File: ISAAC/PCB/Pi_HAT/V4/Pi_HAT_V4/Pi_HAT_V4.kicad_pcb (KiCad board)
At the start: 2 copper layers, 71.7 x 71.3 mm, 29 parts, among them J1 MPU 6050, J2 Pi_GPIO, J3 Display, J4 Conn_01x04_Male, J5 XT60PW-M, J6 Conn_01x04_Male, J8 XT60PW-M, U1 MP2315GJ-Z

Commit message: Updated code: Sorta works
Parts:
- added J7: Pressure Sensor, Connector_PinHeader_2.54mm:PinHeader_1x03_P2.54mm_Vertical, F.Cu at (96.5, 83.9)
- added R1: 2k, Resistor_SMD:R_0805_2012Metric_Pad1.20x1.40mm_HandSolder, B.Cu at (128.4, 96.7)
- added R6: 1k, Resistor_SMD:R_0805_2012Metric_Pad1.20x1.40mm_HandSolder, B.Cu at (130.7, 96.7)
- added R7: 2k, Resistor_SMD:R_0805_2012Metric_Pad1.20x1.40mm_HandSolder, B.Cu at (126.6, 92.2)
- added R8: 1k, Resistor_SMD:R_0805_2012Metric_Pad1.20x1.40mm_HandSolder, B.Cu at (129.0, 92.2)
- added U2: MCP3008-I/SL, .pretty:SOIC127P600X175-16N, B.Cu at (137.5, 93.7)
- moved G*** 3.54 mm to (138.1, 92.5), turned to -45 degrees
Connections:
- C1 pad 1: /Buck Converter/12V -> /12V1
- C2 pad 1: /Buck Converter/12V -> /12V1
- J2 pad 19: unconnected-(J2-Pin_19-Pad19) -> /MOSI
- J2 pad 21: unconnected-(J2-Pin_21-Pad21) -> /MISO
- J2 pad 23: unconnected-(J2-Pin_23-Pad23) -> /SCLK
- J2 pad 24: unconnected-(J2-Pin_24-Pad24) -> /CS
- J4 pad 1: /Buck Converter/12V -> /12V0
- J5 pad 1: /Buck Converter/12V -> /12V0
- J6 pad 1: /Buck Converter/12V -> /12V0
- J8 pad 1: /Buck Converter/12V -> /12V1
- R2 pad 1: /Buck Converter/12V -> /12V1
- U1 pad 2: /Buck Converter/12V -> /12V1
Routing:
- net /Buck Converter/12V: track 189.7 -> 0.00 mm
- net /12V0: track 0.00 -> 138.0 mm
- net /12V1: track 0.00 -> 68.0 mm, vias 0 -> 2
- net GND: track 106.6 -> 150.5 mm
- net /5V: track 85.9 -> 125.7 mm
- net /PS: track 0.00 -> 37.5 mm, vias 0 -> 1
- net /CS: track 0.00 -> 21.6 mm, vias 0 -> 1
- net /SCLK: track 0.00 -> 21.4 mm, vias 0 -> 1
- net /MISO: track 0.00 -> 19.7 mm, vias 0 -> 1
- net /MOSI: track 0.00 -> 18.0 mm, vias 0 -> 1
- net /3.3V: track 68.0 -> 80.1 mm
- net /A-D Converter/4V1: track 0.00 -> 10.1 mm
- net /A-D Converter/4V0: track 0.00 -> 9.49 mm
- added copper zone on B.Cu, net GND
- removed copper zone on F.Cu, net GND
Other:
- board text added: "PI HAT V3 10/21/22 EASY CONTROLS Designed by: Jacob Romeo"
- board text added: "PS"
- board text removed: "PI HAT V4 05/05/23 EASY CONTROLS Designed by: Jacob Romeo"

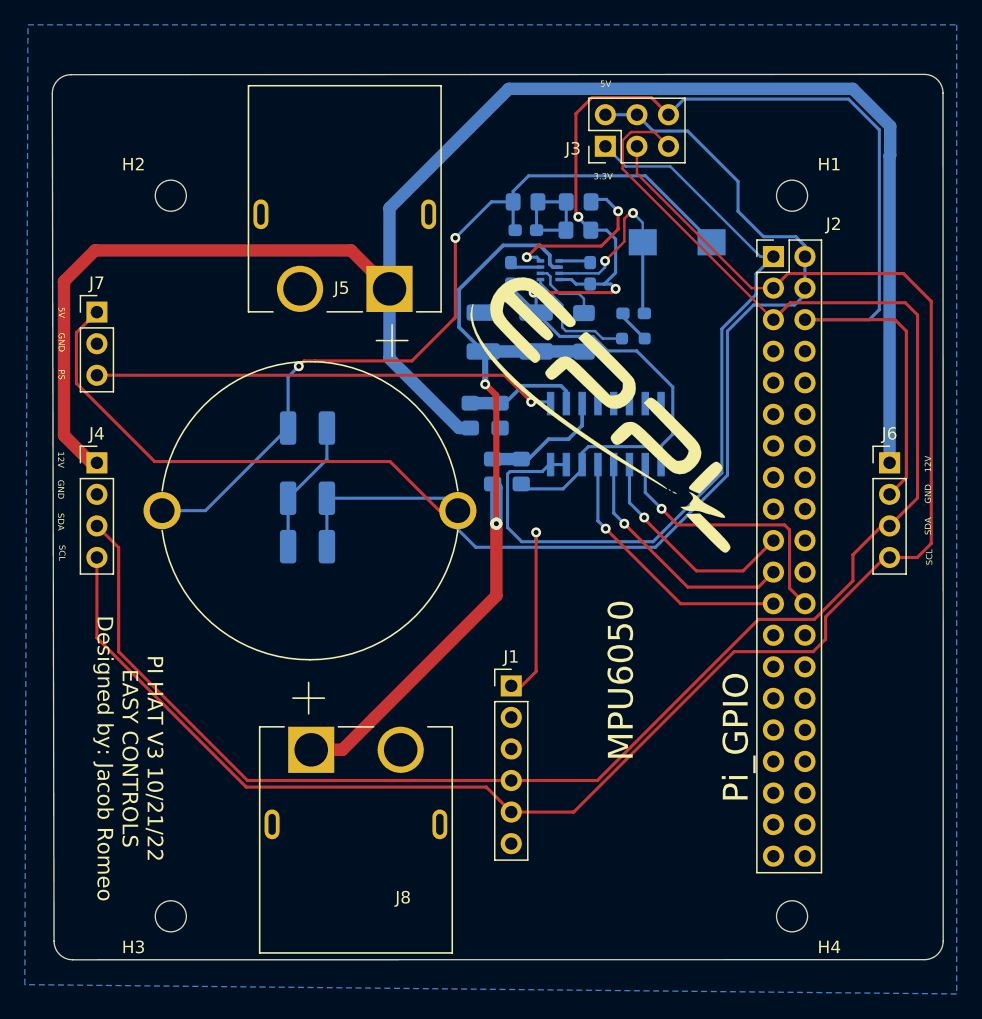
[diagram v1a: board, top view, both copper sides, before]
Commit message: Updated
Started SPARK grant and updated controller and PCB
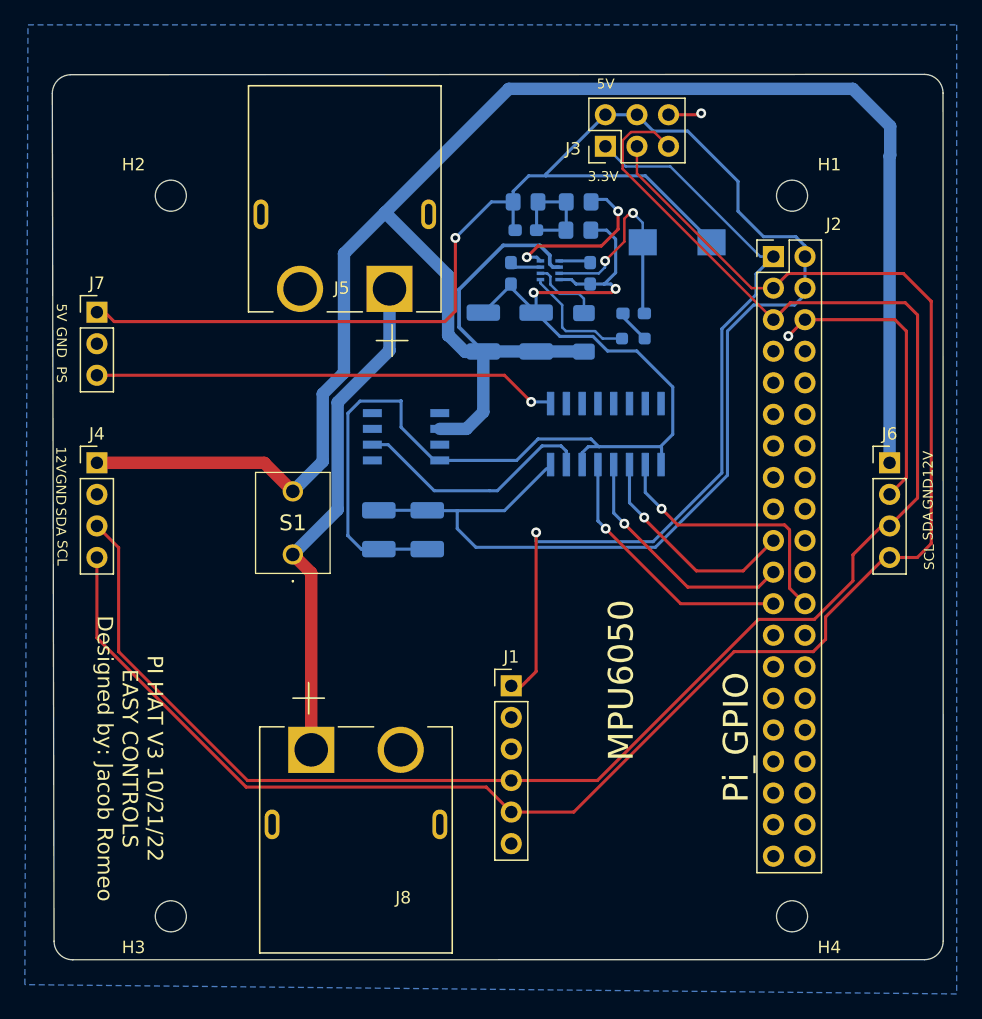
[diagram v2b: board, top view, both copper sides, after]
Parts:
- removed C5: 22u, Capacitor_SMD:C_1210_3225Metric_Pad1.33x2.70mm_HandSolder
- removed G***: LOGO, .pretty:eppl_logo
- removed L2: 220u, .pretty:IND_AIRD-02-151K
- removed R1, R7: 2k, Resistor_SMD:R_0805_2012Metric_Pad1.20x1.40mm_HandSolder
- removed R6, R8: 1k, Resistor_SMD:R_0805_2012Metric_Pad1.20x1.40mm_HandSolder
- added IC1: AD586JRZ-REEL7, refV:SOIC127P600X175-8N, B.Cu at (121.4, 93.9)
- added S1: Switch, refV:2MS6T4B3M2CES, F.Cu at (112.3, 103.4)
- moved C7 9.74 mm to (123.1, 101.4), turned to -90 degrees
- moved C6 6.27 mm to (119.2, 101.4), turned to -90 degrees
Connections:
- C1 pad 1: /12V1 -> /12V
- C2 pad 1: /12V1 -> /12V
- C9 pad 1: Net-(C5-Pad1) -> /5V
- J4 pad 1: /12V0 -> /12V
- J5 pad 1: /12V0 -> /Buck Converter/12Vin
- J6 pad 1: /12V0 -> /12V
- J8 pad 1: /12V1 -> /Buck Converter/12Vin
- L1 pad 2: Net-(C5-Pad1) -> /5V
- R14 pad 1: Net-(C5-Pad1) -> /5V
- R2 pad 1: /12V1 -> /12V
- U1 pad 2: /12V1 -> /12V
- U2 pad 15: /3.3V -> /A-D Converter/ref5V
- U2 pad 16: /3.3V -> /5V
- U2 pad 2: /A-D Converter/4V0 -> unconnected-(U2-CH1-Pad2)
- U2 pad 3: /A-D Converter/4V1 -> unconnected-(U2-CH2-Pad3)
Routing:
- net /12V: track 0.00 -> 164.3 mm
- net /12V0: track 138.0 -> 0.00 mm
- net /12V1: track 68.0 -> 0.00 mm, vias 2 -> 0
- net Net-(C5-Pad1): track 66.6 -> 0.00 mm, vias 2 -> 0
- net /Buck Converter/12Vin: track 0.00 -> 40.9 mm
- net /5V: track 125.7 -> 156.0 mm, vias 0 -> 1
- net GND: track 150.5 -> 121.9 mm, vias 3 -> 4
- net /A-D Converter/ref5V: track 0.00 -> 19.9 mm
- net /3.3V: track 80.1 -> 68.0 mm
- net /A-D Converter/4V1: track 10.1 -> 0.00 mm
- net /A-D Converter/4V0: track 9.49 -> 0.00 mm

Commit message: Updated ISAAC PCB
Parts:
- removed IC1: AD586JRZ-REEL7, refV:SOIC127P600X175-8N
- removed J7: Pressure Sensor, Connector_PinHeader_2.54mm:PinHeader_1x03_P2.54mm_Vertical
- removed U2: MCP3008-I/SL, .pretty:SOIC127P600X175-16N
- J1: value MPU 6050 -> MPU 9250; footprint Connector_PinHeader_2.54mm:PinHeader_1x06_P2.54mm_Vertical -> Connector_PinHeader_2.54mm:PinHeader_1x10_P2.54mm_Vertical
- moved J1 22.6 mm to (128.8, 91.4)
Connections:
- J1 pad 2: unconnected-(J1-Pin_2-Pad2) -> GND
- J1 pad 3: GND -> /SCL
- J1 pad 4: /SCL -> /SDA
- J1 pad 5: /SDA -> unconnected-(J1-Pin_5-Pad5)
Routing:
- net /SCL: track 141.3 -> 54.4 mm
- net /SDA: track 140.0 -> 54.4 mm
- net GND: track 121.9 -> 56.6 mm
- net /5V: track 156.0 -> 96.5 mm, vias 1 -> 0
- net /3.3V: track 68.0 -> 17.2 mm, vias 1 -> 0
- net /PS: track 37.5 -> 0.00 mm, vias 1 -> 0
- net /CS: track 21.6 -> 0.00 mm, vias 1 -> 0
- net /SCLK: track 21.4 -> 0.00 mm, vias 1 -> 0
- net /A-D Converter/ref5V: track 19.9 -> 0.00 mm
- net /MISO: track 19.7 -> 0.00 mm, vias 1 -> 0
- net /MOSI: track 18.0 -> 0.00 mm, vias 1 -> 0
- net /12V: track 164.3 -> 155.3 mm
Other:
- board text added: "MPU 9250"
- board text removed: "MPU6050"

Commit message: updated
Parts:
- added J7: BNO055, Connector_PinHeader_2.54mm:PinHeader_1x06_P2.54mm_Vertical, F.Cu at (128.8, 119.3)
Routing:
- net /SDA: track 54.4 -> 157.8 mm
- net /SCL: track 54.4 -> 148.0 mm
- net /3.3V: track 17.2 -> 79.8 mm
- net GND: track 56.6 -> 89.5 mm, vias 4 -> 6
